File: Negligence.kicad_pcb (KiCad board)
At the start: 2 copper layers, 228.9 x 105.7 mm, 116 parts, among them J1 AVR-ISP-6, SW1 keyboard_parts_KEYSW, SW10 keyboard_parts_KEYSW, SW11 keyboard_parts_KEYSW, SW12 keyboard_parts_KEYSW, SW13 keyboard_parts_KEYSW, SW14 keyboard_parts_KEYSW, SW15 keyboard_parts_KEYSW, SW16 keyboard_parts_KEYSW, SW17 keyboard_parts_KEYSW, SW18 keyboard_parts_KEYSW, SW19 keyboard_parts_KEYSW, SW2 keyboard_parts_KEYSW, SW20 keyboard_parts_KEYSW, SW21 keyboard_parts_KEYSW, SW22 keyboard_parts_KEYSW, SW23 keyboard_parts_KEYSW, SW24 keyboard_parts_KEYSW, SW25 keyboard_parts_KEYSW, SW26 keyboard_parts_KEYSW, SW27 keyboard_parts_KEYSW, SW28 keyboard_parts_KEYSW, SW29 keyboard_parts_KEYSW, SW3 keyboard_parts_KEYSW, SW30 keyboard_parts_KEYSW, SW31 keyboard_parts_KEYSW, SW32 keyboard_parts_KEYSW, SW33 keyboard_parts_KEYSW, SW34 keyboard_parts_KEYSW, SW35 keyboard_parts_KEYSW, SW36 keyboard_parts_KEYSW, SW37 keyboard_parts_KEYSW, SW38 keyboard_parts_KEYSW, SW39 keyboard_parts_KEYSW, SW4 keyboard_parts_KEYSW, SW40 keyboard_parts_KEYSW, SW41 keyboard_parts_KEYSW, SW42 keyboard_parts_KEYSW, SW43 keyboard_parts_KEYSW, SW44 keyboard_parts_KEYSW, SW45 keyboard_parts_KEYSW, SW46 keyboard_parts_KEYSW, SW47 RESET, SW48 BOOT, SW5 keyboard_parts_KEYSW, SW6 keyboard_parts_KEYSW, SW7 keyboard_parts_KEYSW, SW8 keyboard_parts_KEYSW, SW9 keyboard_parts_KEYSW, U1 ATmega328P-PU, Y1 16MHz

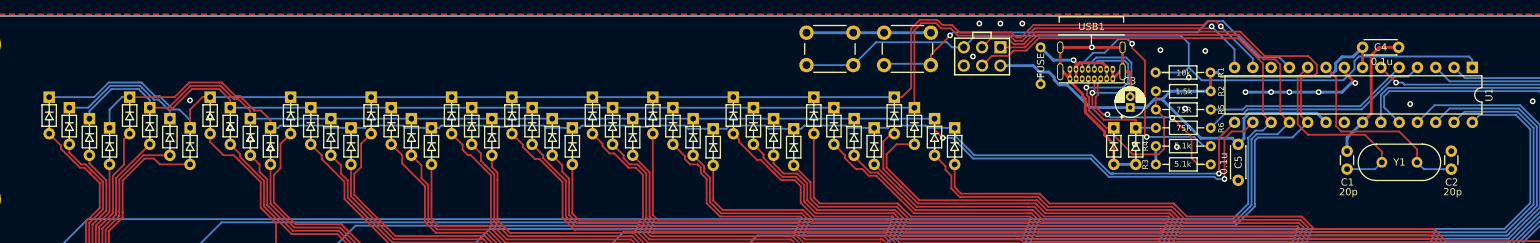
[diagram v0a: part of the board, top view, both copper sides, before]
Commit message: Parts silk screen
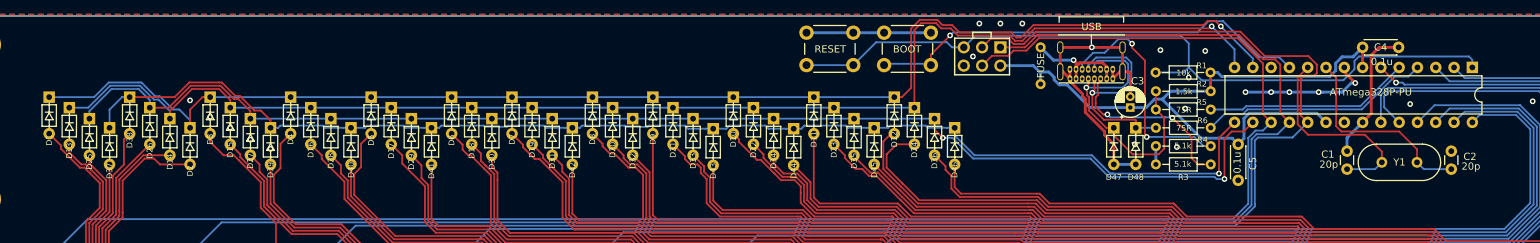
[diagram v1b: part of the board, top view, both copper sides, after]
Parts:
- renumbered U1 to ATmega328P-PU, USB1 to USB
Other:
- board text added: "BOOT"
- board text added: "RESET"

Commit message: Mounting holes
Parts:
- added REF**: MountingHole_2.2mm_M2_Pad, cftkb:MountingHole_2.2mm_M2_Pad, F.Cu at (51.3, 136.5)
- added REF**: MountingHole_2.2mm_M2_Pad, cftkb:MountingHole_2.2mm_M2_Pad, F.Cu at (205.1, 136.5)
- added REF**: MountingHole_2.2mm_M2_Pad, cftkb:MountingHole_2.2mm_M2_Pad, F.Cu at (205.0, 98.3)
- added REF**: MountingHole_2.2mm_M2_Pad, cftkb:MountingHole_2.2mm_M2_Pad, F.Cu at (51.6, 98.4)
- added REF**: MountingHole_2.2mm_M2_Pad, cftkb:MountingHole_2.2mm_M2_Pad, F.Cu at (128.4, 117.5)
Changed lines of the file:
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@@
     (tracks 1231)
     (zones 0)
-    (modules 116)
+    (modules 121)
     (nets 80)
   )
@@
     (add_net VCC)
   )
+  (module cftkb:MountingHole_2.2mm_M2_Pad (layer F.Cu)
+    (at 51.308 136.525)
+    (descr "Mounting Hole 2.2mm, M2")
+    (tags "mounting hole 2.2mm m2")
+    (attr virtual)
+    (fp_text reference REF** (at 0 -3.2) (layer Cmts.User) hide
+      (effects (font (size 1 1) (thickness 0.15)))
+    )
+    (fp_text value MountingHole_2.2mm_M2_Pad (at 0 3.2) (layer F.Fab) hide
+      (effects (font (size 1 1) (thickness 0.15)))
+    )
+    (fp_text user %R (at 0.3 0) (layer F.Fab)
+      (effects (font (size 1 1) (thickness 0.15)))
+    )
+    (fp_circle (center 0 0) (end 2.2 0) (layer Cmts.User) (width 0.15))
+    (fp_circle (center 0 0) (end 2.45 0) (layer F.CrtYd) (width 0.05))
+    (pad 1 thru_hole circle (at 0 0) (size 4.4 4.4) (drill 2.2) (layers *.Cu *.Mask))
+  )
+  (module cftkb:MountingHole_2.2mm_M2_Pad (layer F.Cu)
+    (at 205.105 136.525)
+    (descr "Mounting Hole 2.2mm, M2")
+    (tags "mounting hole 2.2mm m2")
+    (attr virtual)
+    (fp_text reference REF** (at 0 -3.2) (layer Cmts.User) hide
+      (effects (font (size 1 1) (thickness 0.15)))
+    )
+    (fp_text value MountingHole_2.2mm_M2_Pad (at 0 3.2) (layer F.Fab) hide
+      (effects (font (size 1 1) (thickness 0.15)))
+    )
+    (fp_circle (center 0 0) (end 2.45 0) (layer F.CrtYd) (width 0.05))
+    (fp_circle (center 0 0) (end 2.2 0) (layer Cmts.User) (width 0.15))
+    (fp_text user %R (at 0.3 0) (layer F.Fab)
+      (effects (font (size 1 1) (thickness 0.15)))
+    )
+    (pad 1 thru_hole circle (at 0 0) (size 4.4 4.4) (drill 2.2) (layers *.Cu *.Mask))
+  )
+  (module cftkb:MountingHole_2.2mm_M2_Pad (layer F.Cu)
+    (at 204.978 98.298)
+    (descr "Mounting Hole 2.2mm, M2")
+    (tags "mounting hole 2.2mm m2")
+    (attr virtual)
+    (fp_text reference REF** (at 0 -3.2) (layer Cmts.User) hide
+      (effects (font (size 1 1) (thickness 0.15)))
+    )
+    (fp_text value MountingHole_2.2mm_M2_Pad (at 0 3.2) (layer F.Fab) hide
+      (effects (font (size 1 1) (thickness 0.15)))
+    )
+    (fp_text user %R (at 0.3 0) (layer F.Fab)
+      (effects (font (size 1 1) (thickness 0.15)))
+    )
+    (fp_circle (center 0 0) (end 2.2 0) (layer Cmts.User) (width 0.15))
+    (fp_circle (center 0 0) (end 2.45 0) (layer F.CrtYd) (width 0.05))
+    (pad 1 thru_hole circle (at 0 0) (size 4.4 4.4) (drill 2.2) (layers *.Cu *.Mask))
+  )
+  (module cftkb:MountingHole_2.2mm_M2_Pad (layer F.Cu)
+    (at 51.562 98.425)
+    (descr "Mounting Hole 2.2mm, M2")
+    (tags "mounting hole 2.2mm m2")
+    (attr virtual)
+    (fp_text reference REF** (at 0 -3.2) (layer Cmts.User) hide
+      (effects (font (size 1 1) (thickness 0.15)))
+    )
+    (fp_text value MountingHole_2.2mm_M2_Pad (at 0 3.2) (layer F.Fab) hide
+      (effects (font (size 1 1) (thickness 0.15)))
+    )
+    (fp_circle (center 0 0) (end 2.45 0) (layer F.CrtYd) (width 0.05))
+    (fp_circle (center 0 0) (end 2.2 0) (layer Cmts.User) (width 0.15))
+    (fp_text user %R (at 0.3 0) (layer F.Fab)
+      (effects (font (size 1 1) (thickness 0.15)))
+    )
+    (pad 1 thru_hole circle (at 0 0) (size 4.4 4.4) (drill 2.2) (layers *.Cu *.Mask))
+  )
+  (module cftkb:MountingHole_2.2mm_M2_Pad (layer F.Cu)
+    (at 128.397 117.475)
+    (descr "Mounting Hole 2.2mm, M2")
+    (tags "mounting hole 2.2mm m2")
+    (attr virtual)
+    (fp_text reference REF** (at 0 -3.2) (layer Cmts.User) hide
+      (effects (font (size 1 1) (thickness 0.15)))
+    )
+    (fp_text value MountingHole_2.2mm_M2_Pad (at 0 3.2) (layer F.Fab) hide
+      (effects (font (size 1 1) (thickness 0.15)))
+    )
+    (fp_text user %R (at 0.3 0) (layer F.Fab)
+      (effects (font (size 1 1) (thickness 0.15)))
+    )
+    (fp_circle (center 0 0) (end 2.2 0) (layer Cmts.User) (width 0.15))
+    (fp_circle (center 0 0) (end 2.45 0) (layer F.CrtYd) (width 0.05))
+    (pad 1 thru_hole circle (at 0 0) (size 4.4 4.4) (drill 2.2) (layers *.Cu *.Mask))
+  )
   (module Package_DIP:DIP-28_W7.62mm (layer F.Cu)
